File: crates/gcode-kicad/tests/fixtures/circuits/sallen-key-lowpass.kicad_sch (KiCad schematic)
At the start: 5 parts, among them U1 LM321

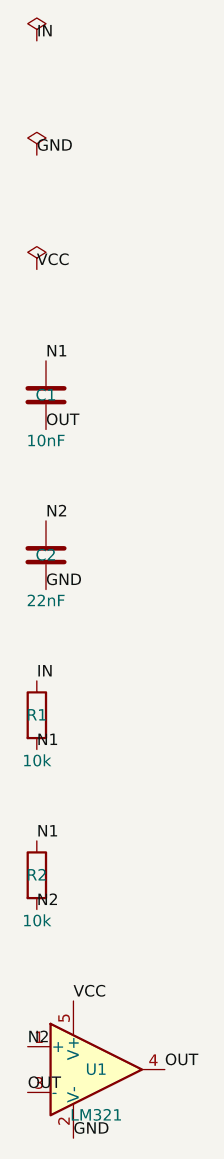
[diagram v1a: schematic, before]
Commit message: R1: gcode-sim crate — SPICE netlist generation, ngspice driver, metric analysis
New crate crates/gcode-sim:
- models: lib_id -> SPICE card + behavioural macromodels (LM321 single-pole
  opamp, Q_NMOS level-1, LED, L7805, thermistor); unknown devices are rejected
- netlist: deterministic deck from NetlistIr; GND -> node 0, sanitised node names
  with collision detection, stimuli from the analysis config, wrdata control block
- runner: ngspice probe/version gate, batch execution, waveform retrieval parsed
  BY COLUMN NAME (which is what makes .op's placeholder scale column harmless)
- analysis: pure metric extraction (dc, gain, shape-aware -3dB, rise time,
  ripple, min/max) plus expectation checking with Chinese explanations
- artifacts: deterministic CSV and dependency-free SVG (Bode + time domain)
- recipes: 11 recipes over all 10 catalog circuits with analytically derived
  expectations and documented tolerances

Real findings from actually simulating (all fixed):
- non-inverting-amp was wired for gain 1.11, not 10.1 (feedback resistors swapped)
- MOSFETs need the M card, not Q (Q is a BJT); bulk ties to source
- ngspice level-1 MOS rejects Cgs/Cgd (wants CGSO/CGDO)
- ngspice vp() returns radians, not degrees
- with the switch off, the drain is a floating node; measure the supply side
- Sallen-Key Q was 0.34 (overdamped) -> values swapped for Q~0.74
- thermistor value must be numeric to be simulatable

Acceptance: 11/11 recipes, 12/12 metrics PASS against ngspice-42; R0 still
10/10 KR1 and 146 workspace tests green.
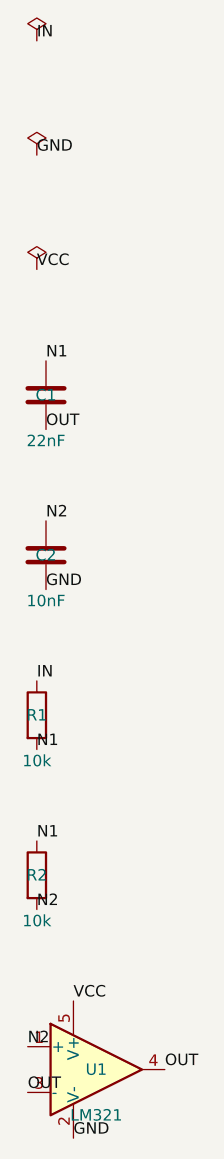
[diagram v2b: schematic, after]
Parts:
- C1: value 10nF -> 22nF
- C2: value 22nF -> 10nF
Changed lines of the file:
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@@
     (instances (project
   "gcode"
-  (path "/5782830c-dd13-587d-9cdf-02b44439b44e" (reference "#FLG1") (unit 1))
+  (path "/1b35cfd0-5ba1-5837-b4a7-0e2c0dbaeaf8" (reference "#FLG1") (unit 1))
 ))
   )
@@
     (instances (project
   "gcode"
-  (path "/5782830c-dd13-587d-9cdf-02b44439b44e" (reference "#FLG2") (unit 1))
+  (path "/1b35cfd0-5ba1-5837-b4a7-0e2c0dbaeaf8" (reference "#FLG2") (unit 1))
 ))
   )
@@
     (instances (project
   "gcode"
-  (path "/5782830c-dd13-587d-9cdf-02b44439b44e" (reference "#FLG3") (unit 1))
+  (path "/1b35cfd0-5ba1-5837-b4a7-0e2c0dbaeaf8" (reference "#FLG3") (unit 1))
 ))
   )
@@
     (property
       "Value"
-      "10nF"
+      "22nF"
       (at 78.232 97.79 0)
       (show_name no)
@@
     (instances (project
   "gcode"
-  (path "/5782830c-dd13-587d-9cdf-02b44439b44e" (reference "C1") (unit 1))
+  (path "/1b35cfd0-5ba1-5837-b4a7-0e2c0dbaeaf8" (reference "C1") (unit 1))
 ))
   )
@@
     (property
       "Value"
-      "22nF"
+      "10nF"
       (at 78.232 115.57 0)
       (show_name no)
@@
     (instances (project
   "gcode"
-  (path "/5782830c-dd13-587d-9cdf-02b44439b44e" (reference "C2") (unit 1))
+  (path "/1b35cfd0-5ba1-5837-b4a7-0e2c0dbaeaf8" (reference "C2") (unit 1))
 ))
   )
@@
     (instances (project
   "gcode"
-  (path "/5782830c-dd13-587d-9cdf-02b44439b44e" (reference "R1") (unit 1))
+  (path "/1b35cfd0-5ba1-5837-b4a7-0e2c0dbaeaf8" (reference "R1") (unit 1))
 ))
   )
@@
     (instances (project
   "gcode"
-  (path "/5782830c-dd13-587d-9cdf-02b44439b44e" (reference "R2") (unit 1))
+  (path "/1b35cfd0-5ba1-5837-b4a7-0e2c0dbaeaf8" (reference "R2") (unit 1))
 ))
   )
@@
     (instances (project
   "gcode"
-  (path "/5782830c-dd13-587d-9cdf-02b44439b44e" (reference "U1") (unit 1))
-))
-  )
+  (path "/1b35cfd0-5ba1-5837-b4a7-0e2c0dbaeaf8" (reference "U1") (unit 1))
+))
+  )
